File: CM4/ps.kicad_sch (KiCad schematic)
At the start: 45 parts, among them J1 USB_B, J2 Conn_01x02, J3 Conn_01x02, Q1 EMH3, U2 NCP114ASN330T1G, U3 BQ25887RGET, U4 MAX17643, U5 ATTINY85-20PU, U6 TQ2SA-L2-3V-Z-Remake

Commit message: Added USB Hub Contoler and usb port internal and external
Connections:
- net GND renamed Earth_Clean
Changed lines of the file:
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@@
   (junction (at 102.235 81.28) (diameter 1.016) (color 0 0 0 0))
   (junction (at 104.775 86.36) (diameter 1.016) (color 0 0 0 0))
+  (junction (at 104.775 92.075) (diameter 1.016) (color 0 0 0 0))
   (junction (at 115.57 26.035) (diameter 1.016) (color 0 0 0 0))
   (junction (at 121.285 52.705) (diameter 1.016) (color 0 0 0 0))
@@
     (pin "2")
   )
+  (symbol (lib_id "power:Earth_Clean") (at 104.775 92.075 0) (unit 1)
+    (in_bom yes) (on_board yes)
+    (property "Reference" "#PWR0130" (id 0) (at 111.125 92.075 0)
+      (effects (font (size 1.27 1.27)) hide)
+    )
+    (property "Value" "Earth_Clean" (id 1) (at 112.395 95.885 0)
+      (effects (font (size 1.27 1.27)) hide)
+    )
+    (property "Footprint" "" (id 2) (at 104.775 93.345 0)
+      (effects (font (size 1.27 1.27)) hide)
+    )
+    (property "Datasheet" "~" (id 3) (at 104.775 93.345 0)
+      (effects (font (size 1.27 1.27)) hide)
+    )
+    (pin "1")
+  )
   (symbol (lib_id "Diode:1N4148W") (at 140.208 140.462 270) (unit 1)

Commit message: Added Keyboard matrix controller and indicator leds
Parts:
- added C16, C17: 10 uF, Capacitor_SMD:C_1206_3216Metric, symbol Device:C_Small
- added U8: TLV740P, Package_TO_SOT_SMD:SOT-23-5_HandSoldering, symbol teensy:TLV740P
- D81, D82: footprint LED_SMD:LED_2010_5025Metric -> LED_SMD:LED_1206_3216Metric_Pad1.42x1.75mm_HandSolder
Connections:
- net +5: now also C16.1, U8.1 (IN), U8.3 (EN)
- net Earth_Clean: now also C16.2, C17.1, U8.2 (GND)
- new net +1: C17.2, U8.5 (OUT)
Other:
- note added: "+1 V Regulator"
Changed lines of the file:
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@@
   (junction (at 104.775 86.36) (diameter 1.016) (color 0 0 0 0))
   (junction (at 104.775 92.075) (diameter 1.016) (color 0 0 0 0))
+  (junction (at 113.665 173.355) (diameter 1.016) (color 0 0 0 0))
   (junction (at 115.57 26.035) (diameter 1.016) (color 0 0 0 0))
+  (junction (at 115.57 173.355) (diameter 1.016) (color 0 0 0 0))
   (junction (at 121.285 52.705) (diameter 1.016) (color 0 0 0 0))
   (junction (at 144.018 144.272) (diameter 1.016) (color 0 0 0 0))
@@
     (stroke (width 0) (type solid) (color 0 0 0 0))
   )
+  (wire (pts (xy 113.03 173.355) (xy 113.665 173.355))
+    (stroke (width 0) (type solid) (color 0 0 0 0))
+  )
+  (wire (pts (xy 113.665 173.355) (xy 115.57 173.355))
+    (stroke (width 0) (type solid) (color 0 0 0 0))
+  )
   (wire (pts (xy 115.57 26.035) (xy 118.11 26.035))
+    (stroke (width 0) (type solid) (color 0 0 0 0))
+  )
+  (wire (pts (xy 115.57 173.355) (xy 115.57 175.895))
     (stroke (width 0) (type solid) (color 0 0 0 0))
   )
@@
     (effects (font (size 1.27 1.27)) (justify left bottom))
   )
+  (text "+1 V Regulator" (at 128.905 167.005 180)
+    (effects (font (size 1.27 1.27)) (justify right bottom))
+  )
   (text "The pi can pull a max of 1.5A @ 5v so 7W \n" (at 172.085 20.955 180)
     (effects (font (size 1.27 1.27)) (justify right bottom))
@@
     )
   )
+  (global_label "+5" (shape input) (at 113.03 173.355 180)
+    (effects (font (size 1.27 1.27)) (justify right))
+    (property "Intersheet References" "${INTERSHEET_REFS}" (id 0) (at 107.835 173.2756 0)
+      (effects (font (size 1.27 1.27)) (justify right) hide)
+    )
+  )
   (global_label "!PowerGood" (shape input) (at 121.285 62.865 0)
     (effects (font (size 1.27 1.27)) (justify left))
@@
     )
   )
+  (global_label "+1" (shape input) (at 128.905 173.355 0)
+    (effects (font (size 1.27 1.27)) (justify left))
+    (property "Intersheet References" "${INTERSHEET_REFS}" (id 0) (at 134.1 173.2756 0)
+      (effects (font (size 1.27 1.27)) (justify left) hide)
+    )
+  )
   (global_label "SetPowerOFF" (shape input) (at 133.858 149.352 180)
     (effects (font (size 1.27 1.27)) (justify right))
@@
     (pin "1")
   )
+  (symbol (lib_id "power:GND") (at 113.665 178.435 0) (unit 1)
+    (in_bom yes) (on_board yes)
+    (property "Reference" "#PWR0142" (id 0) (at 113.665 184.785 0)
+      (effects (font (size 1.27 1.27)) hide)
+    )
+    (property "Value" "GND" (id 1) (at 113.665 182.7594 0))
+    (property "Footprint" "" (id 2) (at 113.665 178.435 0)
+      (effects (font (size 1.27 1.27)) hide)
+    )
+    (property "Datasheet" "" (id 3) (at 113.665 178.435 0)
+      (effects (font (size 1.27 1.27)) hide)
+    )
+    (pin "1")
+  )
   (symbol (lib_id "power:GND") (at 115.57 26.035 180) (unit 1)
     (in_bom yes) (on_board yes)
@@
     )
     (property "Datasheet" "" (id 3) (at 115.57 26.035 0)
+      (effects (font (size 1.27 1.27)) hide)
+    )
+    (pin "1")
+  )
+  (symbol (lib_id "power:GND") (at 122.555 184.15 0) (unit 1)
+    (in_bom yes) (on_board yes)
+    (property "Reference" "#PWR0140" (id 0) (at 122.555 190.5 0)
+      (effects (font (size 1.27 1.27)) hide)
+    )
+    (property "Value" "GND" (id 1) (at 122.555 188.4744 0))
+    (property "Footprint" "" (id 2) (at 122.555 184.15 0)
+      (effects (font (size 1.27 1.27)) hide)
+    )
+    (property "Datasheet" "" (id 3) (at 122.555 184.15 0)
+      (effects (font (size 1.27 1.27)) hide)
+    )
+    (pin "1")
+  )
+  (symbol (lib_id "power:GND") (at 128.905 178.435 0) (unit 1)
+    (in_bom yes) (on_board yes)
+    (property "Reference" "#PWR0141" (id 0) (at 128.905 184.785 0)
+      (effects (font (size 1.27 1.27)) hide)
+    )
+    (property "Value" "GND" (id 1) (at 128.905 182.7594 0))
+    (property "Footprint" "" (id 2) (at 128.905 178.435 0)
+      (effects (font (size 1.27 1.27)) hide)
+    )
+    (property "Datasheet" "" (id 3) (at 128.905 178.435 0)
       (effects (font (size 1.27 1.27)) hide)
     )
@@
     (pin "2")
   )
+  (symbol (lib_id "Device:C_Small") (at 113.665 175.895 0) (unit 1)
+    (in_bom yes) (on_board yes)
+    (property "Reference" "C16" (id 0) (at 105.5752 177.8011 0)
+      (effects (font (size 1.27 1.27)) (justify left))
+    )
+    (property "Value" "10 uF" (id 1) (at 105.8292 176.1628 0)
+      (effects (font (size 1.27 1.27)) (justify left))
+    )
+    (property "Footprint" "Capacitor_SMD:C_1206_3216Metric" (id 2) (at 113.665 175.895 0)
+      (effects (font (size 1.27 1.27)) hide)
+    )
+    (property "Datasheet" "~" (id 3) (at 113.665 175.895 0)
+      (effects (font (size 1.27 1.27)) hide)
+    )
+    (pin "1")
+    (pin "2")
+  )
+  (symbol (lib_id "Device:C_Small") (at 128.905 175.895 180) (unit 1)
+    (in_bom yes) (on_board yes)
+    (property "Reference" "C17" (id 0) (at 136.9948 173.9889 0)
+      (effects (font (size 1.27 1.27)) (justify left))
+    )
+    (property "Value" "10 uF" (id 1) (at 136.7408 175.6272 0)
+      (effects (font (size 1.27 1.27)) (justify left))
+    )
+    (property "Footprint" "Capacitor_SMD:C_1206_3216Metric" (id 2) (at 128.905 175.895 0)
+      (effects (font (size 1.27 1.27)) hide)
+    )
+    (property "Datasheet" "~" (id 3) (at 128.905 175.895 0)
+      (effects (font (size 1.27 1.27)) hide)
+    )
+    (pin "1")
+    (pin "2")
+  )
   (symbol (lib_id "Device:C_Small") (at 186.055 55.245 180) (unit 1)
     (in_bom yes) (on_board yes)
@@
     (property "Reference" "D81" (id 0) (at 144.5895 60.0668 0))
     (property "Value" "CHG/ERR" (id 1) (at 142.0495 62.3655 0))
-    (property "Footprint" "LED_SMD:LED_2010_5025Metric" (id 2) (at 144.78 64.77 0)
+    (property "Footprint" "LED_SMD:LED_1206_3216Metric_Pad1.42x1.75mm_HandSolder" (id 2) (at 144.78 64.77 0)
       (effects (font (size 1.27 1.27)) hide)
     )
@@
     (property "Reference" "D82" (id 0) (at 204.978 107.696 0))
     (property "Value" "PWR IND" (id 1) (at 204.978 110.236 0))
-    (property "Footprint" "LED_SMD:LED_2010_5025Metric" (id 2) (at 206.502 111.252 0)
+    (property "Footprint" "LED_SMD:LED_1206_3216Metric_Pad1.42x1.75mm_HandSolder" (id 2) (at 206.502 111.252 0)
       (effects (font (size 1.27 1.27)) hide)
     )
@@
     (pin "3")
     (pin "4")
+    (pin "5")
+  )
+  (symbol (lib_id "teensy:TLV740P") (at 123.19 178.435 0) (unit 1)
+    (in_bom yes) (on_board yes)
+    (property "Reference" "U8" (id 0) (at 122.2375 168.0676 0))
+    (property "Value" "TLV740P" (id 1) (at 122.2375 170.3663 0))
+    (property "Footprint" "Package_TO_SOT_SMD:SOT-23-5_HandSoldering" (id 2) (at 109.855 151.765 0)
+      (effects (font (size 1.27 1.27)) hide)
+    )
+    (property "Datasheet" "" (id 3) (at 109.855 151.765 0)
+      (effects (font (size 1.27 1.27)) hide)
+    )
+    (pin "1")
+    (pin "2")
+    (pin "3")
+    (pin "4")

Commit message: Cleaned Up the Matrix contolller
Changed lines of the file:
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@@
     (stroke (width 0) (type dash) (color 0 0 0 0))
   )
-  (image (at 32.766 104.267) (scale 0.387142)
+  (image (at 56.261 141.097) (scale 0.919911)
     (data
       iVBORw0KGgoAAAANSUhEUgAAA6gAAAMTCAMAAACbksqsAAAAA3NCSVQICAjb4U/gAAABX1BMVEX/
@@
     (effects (font (size 1.27 1.27)) (justify right bottom))
   )
+  (label "FB" (at 220.98 46.99 0)
+    (effects (font (size 1.27 1.27)) (justify left bottom))
+  )
+  (label "FB" (at 257.175 51.435 0)
+    (effects (font (size 1.27 1.27)) (justify left bottom))
+  )
   (global_label "chargeDisable" (shape input) (at 54.61 60.325 180)
     (effects (font (size 1.27 1.27)) (justify right))
@@
     )
   )
-  (global_label "FB" (shape input) (at 220.98 46.99 0)
-    (effects (font (size 1.27 1.27)) (justify left))
-    (property "Intersheet References" "${INTERSHEET_REFS}" (id 0) (at 225.7517 46.9106 0)
-      (effects (font (size 1.27 1.27)) (justify left) hide)
-    )
-  )
   (global_label "batCell+" (shape input) (at 225.552 103.632 90)
     (effects (font (size 1.27 1.27)) (justify left))
@@
       (effects (font (size 1.27 1.27)) (justify left) hide)
     )
-  )
-  (global_label "FB" (shape input) (at 257.175 51.435 0)
-    (effects (font (size 1.27 1.27)) (justify left))
-    (property "Intersheet References" "${INTERSHEET_REFS}" (id 0) (at 261.9467 51.3556 0)
-      (effects (font (size 1.27 1.27)) (justify left) hide)
-    )

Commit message: added battery connecoectors and emmcbootdisable jumpper
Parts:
- J2: value Conn_01x02 -> Bat0; footprint Connector_JST:JST_PH_B2B-PH-K_1x02_P2.00mm_Vertical -> Connector_PinHeader_2.54mm:PinHeader_1x02_P2.54mm_Horizontal
- J3: value Conn_01x02 -> Bat1; footprint Connector_JST:JST_PH_B2B-PH-K_1x02_P2.00mm_Vertical -> Connector_PinHeader_2.54mm:PinHeader_1x02_P2.54mm_Horizontal
- TH1: value 10K -> 10K Thermister; footprint Connector_PinSocket_2.54mm:PinSocket_1x02_P2.54mm_Vertical -> Connector_PinHeader_2.54mm:PinHeader_1x02_P2.54mm_Horizontal
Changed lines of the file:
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@@
       (effects (font (size 1.27 1.27)) (justify left))
     )
-    (property "Value" "Conn_01x02" (id 1) (at 112.395 84.4549 0)
+    (property "Value" "Bat1" (id 1) (at 112.395 84.4549 0)
       (effects (font (size 1.27 1.27)) (justify left))
     )
-    (property "Footprint" "Connector_JST:JST_PH_B2B-PH-K_1x02_P2.00mm_Vertical" (id 2) (at 109.855 81.28 0)
+    (property "Footprint" "Connector_PinHeader_2.54mm:PinHeader_1x02_P2.54mm_Horizontal" (id 2) (at 109.855 81.28 0)
       (effects (font (size 1.27 1.27)) hide)
     )
@@
       (effects (font (size 1.27 1.27)) (justify left))
     )
-    (property "Value" "Conn_01x02" (id 1) (at 112.395 92.7099 0)
+    (property "Value" "Bat0" (id 1) (at 112.395 92.7099 0)
       (effects (font (size 1.27 1.27)) (justify left))
     )
-    (property "Footprint" "Connector_JST:JST_PH_B2B-PH-K_1x02_P2.00mm_Vertical" (id 2) (at 109.855 89.535 0)
+    (property "Footprint" "Connector_PinHeader_2.54mm:PinHeader_1x02_P2.54mm_Horizontal" (id 2) (at 109.855 89.535 0)
       (effects (font (size 1.27 1.27)) hide)
     )
@@
       (effects (font (size 1.27 1.27)) (justify left))
     )
-    (property "Value" "10K" (id 1) (at 26.5431 78.3728 0)
+    (property "Value" "10K Thermister" (id 1) (at 26.5431 78.3728 0)
       (effects (font (size 1.27 1.27)) (justify left))
     )
-    (property "Footprint" "Connector_PinSocket_2.54mm:PinSocket_1x02_P2.54mm_Vertical" (id 2) (at 24.13 75.565 0)
+    (property "Footprint" "Connector_PinHeader_2.54mm:PinHeader_1x02_P2.54mm_Horizontal" (id 2) (at 24.13 75.565 0)
       (effects (font (size 1.27 1.27)) hide)
     )

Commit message: Started the "fun" of routing
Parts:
- kbPowerButton1: footprint Button_Switch_SMD:SW_SPST_B3SL-1002P -> lib:Kbpad
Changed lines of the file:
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@@
     )
     (property "Value" "CTRL" (id 1) (at 186.69 112.268 0))
-    (property "Footprint" "Button_Switch_SMD:SW_SPST_B3SL-1002P" (id 2) (at 193.802 111.252 0)
+    (property "Footprint" "lib:Kbpad" (id 2) (at 193.802 111.252 0)
       (effects (font (size 1.27 1.27)) hide)
     )

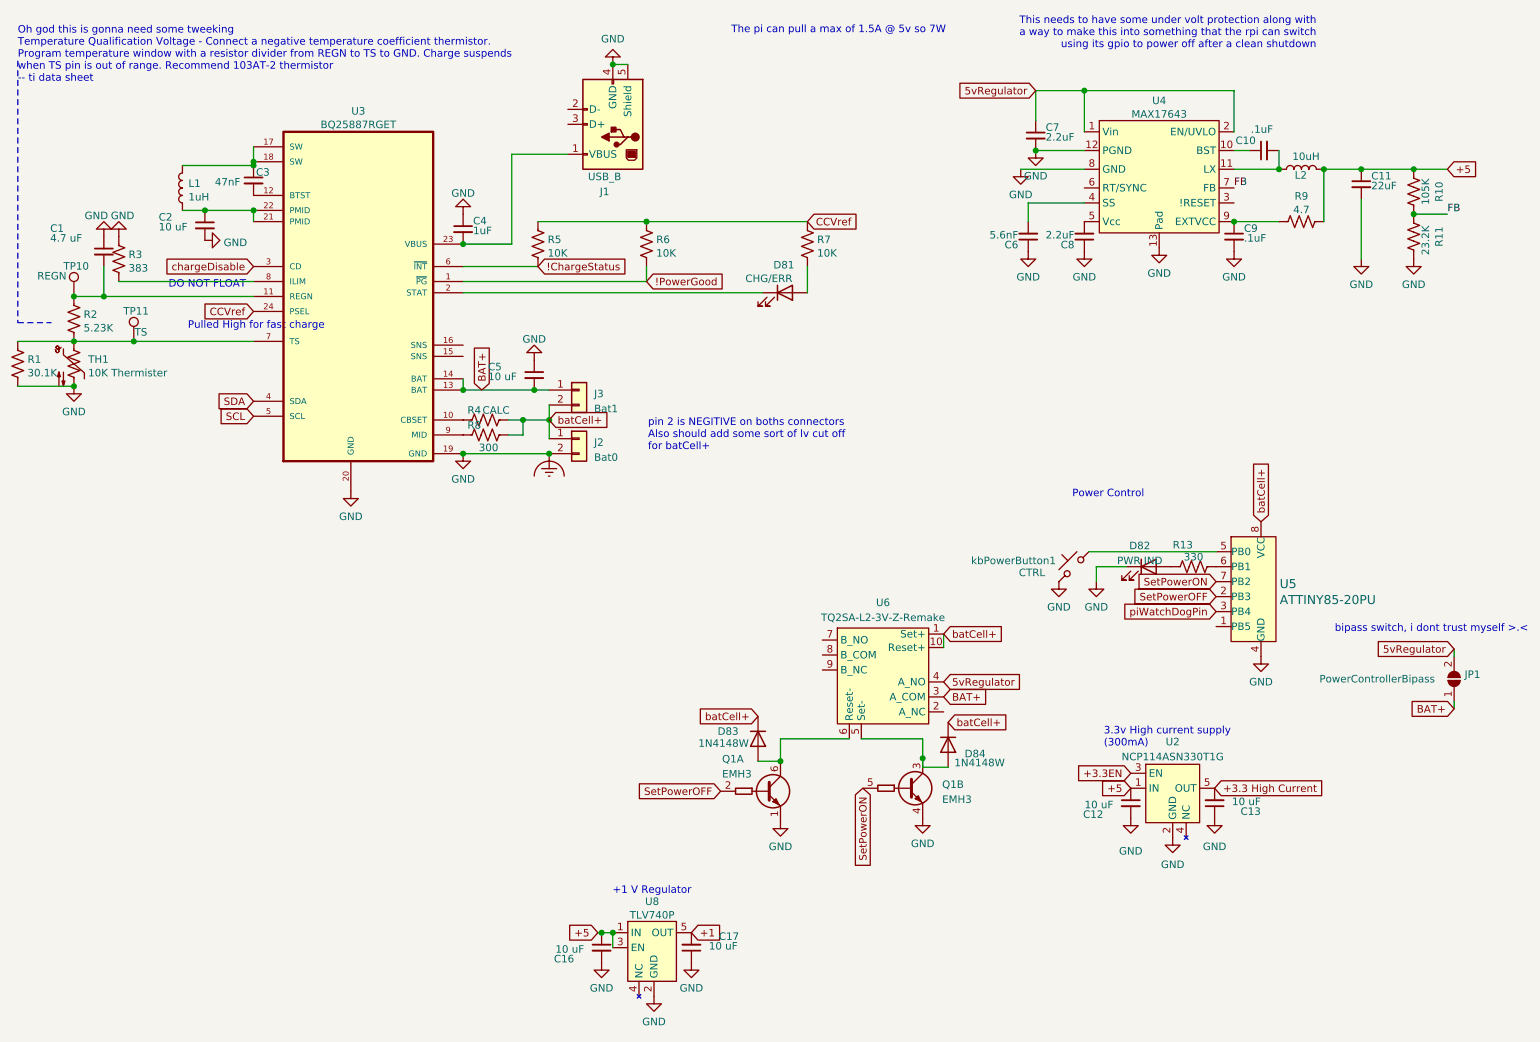
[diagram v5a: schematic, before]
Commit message: Everything is routed
Just waiting on display to finsh routing that, then its time to get some pcbs on the way and cross my fingers that i dont cook a cm4 >.<
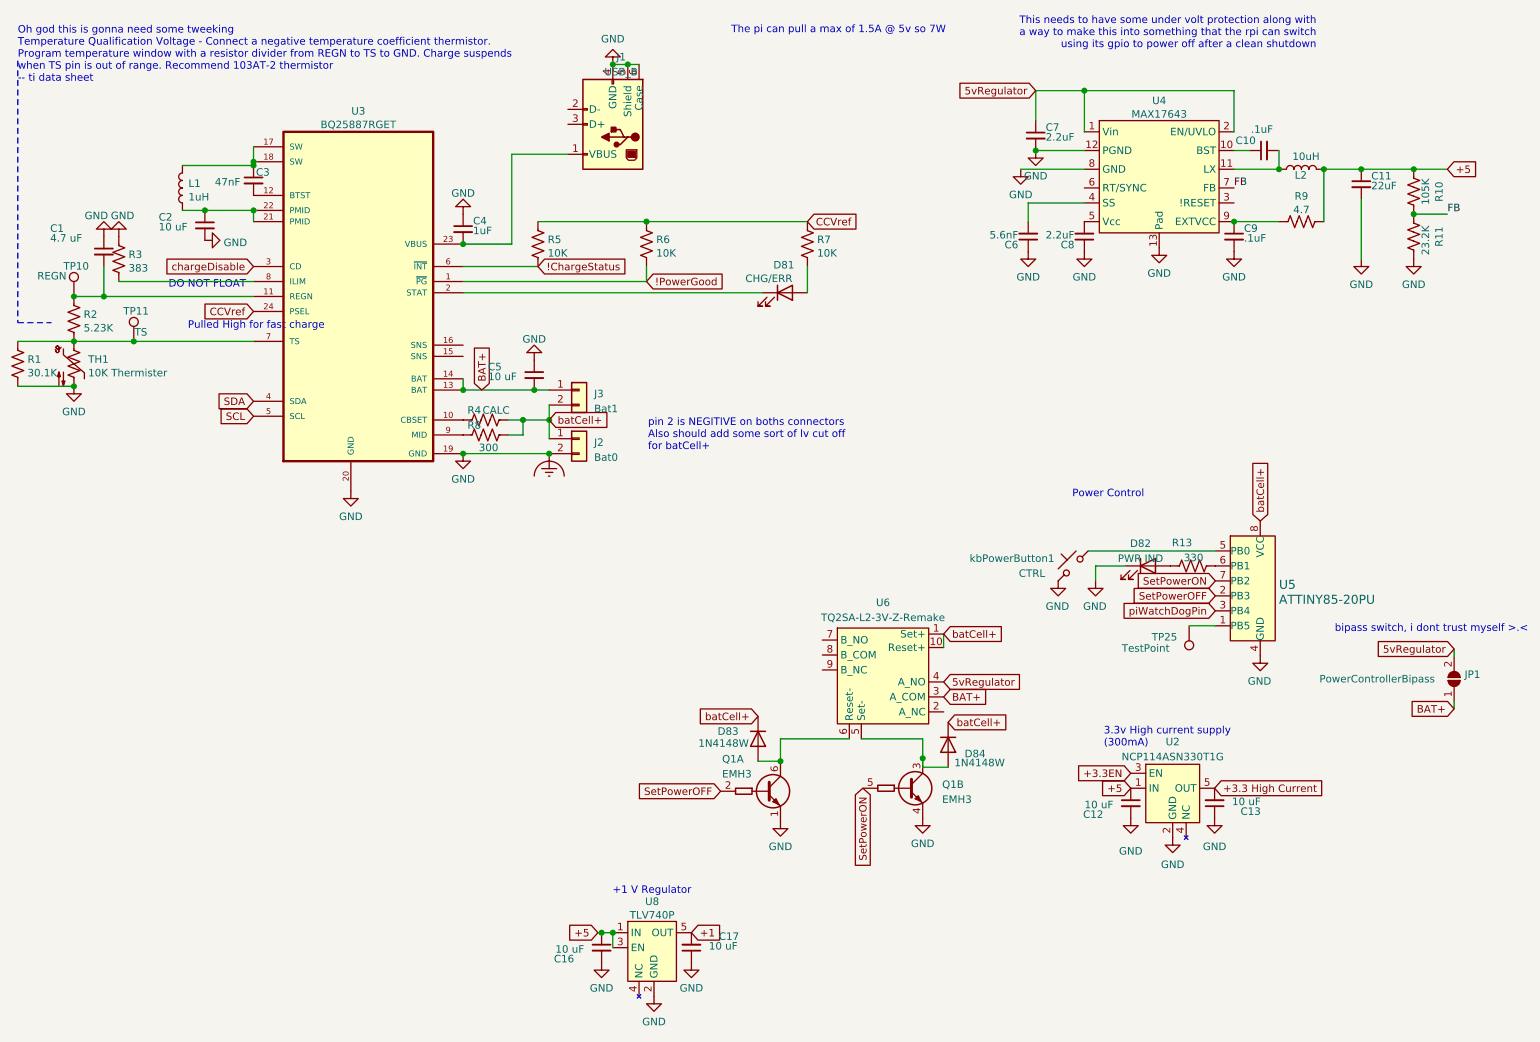
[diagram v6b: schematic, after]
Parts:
- added TP25: TestPoint, TestPoint:TestPoint_Pad_D1.0mm, symbol Connector:TestPoint
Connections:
- net Earth_Clean: now also J1.6 (Case)
- net at U5.1 (PB5): now also TP25.1

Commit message: Compleated REV001
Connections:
- net +5: now also U6.8 (B_COM)
- net relay_no_b: now reaches U6.7 (B_NO)
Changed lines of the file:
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@@
+    )
+  )
+  (global_label "relay_no_b" (shape input) (at 151.13 123.698 180)
+    (effects (font (size 1.27 1.27)) (justify right))
+    (property "Intersheet References" "${INTERSHEET_REFS}" (id 0) (at 138.6779 123.6186 0)
+      (effects (font (size 1.27 1.27)) (justify right) hide)
+    )
+  )
+  (global_label "+5" (shape input) (at 151.13 126.238 180)
+    (effects (font (size 1.27 1.27)) (justify right))
+    (property "Intersheet References" "${INTERSHEET_REFS}" (id 0) (at 145.935 126.1586 0)
+      (effects (font (size 1.27 1.27)) (justify right) hide)
     )
   )
